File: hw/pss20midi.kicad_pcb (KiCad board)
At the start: 2 copper layers, 293.5 x 44 mm, 90 parts, among them J1 AVR-ISP, J2 Power in, J3 MIDI out, J4 keypad3, SW1 SW_Push, SW10 SW_Push, SW11 SW_Push, SW12 SW_Push, SW13 SW_Push, SW14 SW_Push, SW15 SW_Push, SW16 SW_Push, SW17 SW_Push, SW18 SW_Push, SW19 SW_Push, SW2 SW_Push, SW20 SW_Push, SW21 SW_Push, SW22 SW_Push, SW23 SW_Push, SW24 SW_Push, SW25 SW_Push, SW26 SW_Push, SW27 SW_Push, SW28 SW_Push, SW29 SW_Push, SW3 SW_Push, SW30 SW_Push, SW31 SW_Push, SW32 SW_Push, SW4 SW_Push, SW5 SW_Push, SW6 SW_Push, SW7 SW_Push, SW8 SW_Push, SW9 SW_Push, U1 ATmega328PB, U2 74HC153, U3 74HC153, U4 74HC153, U5 74HC153, U6 MAX232, Y1 4MHz

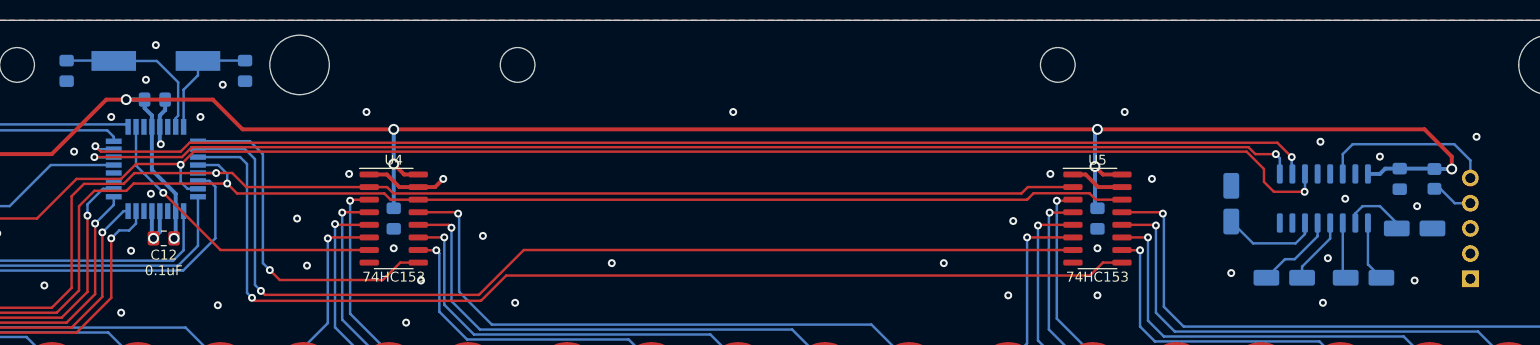
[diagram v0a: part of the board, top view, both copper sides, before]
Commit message: fixed MIDI voltage and polarity mistake
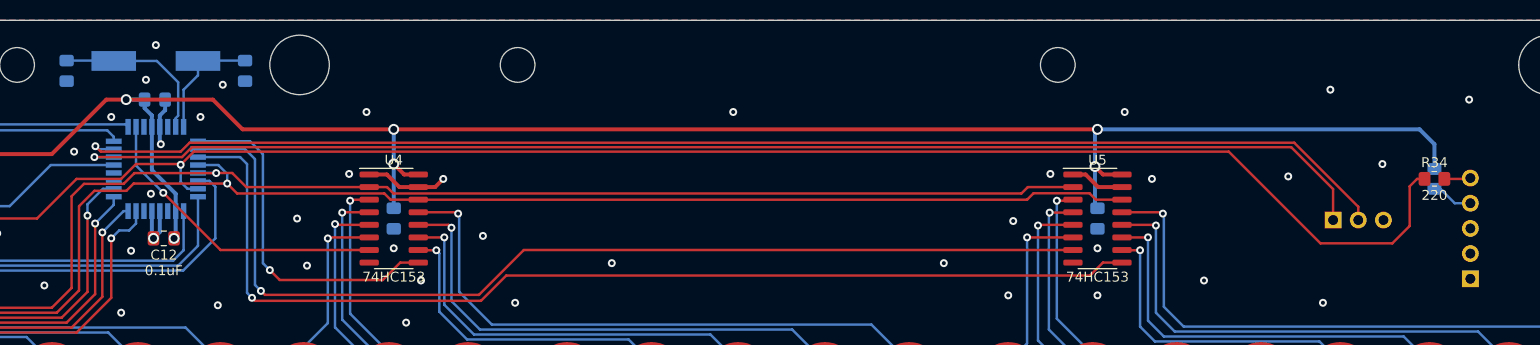
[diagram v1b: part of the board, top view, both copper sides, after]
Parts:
- removed C13: 0.1uF, Capacitor_SMD:C_0805_2012Metric_Pad1.18x1.45mm_HandSolder
- removed C3, C4, C5, C6: 1uF, Capacitor_SMD:CP_Elec_4x5.4
- removed U6: MAX232, Package_SO:SOIC-16_3.9x9.9mm_P1.27mm
- added J5: dbgcon, Connector_PinSocket_2.54mm:PinSocket_1x03_P2.54mm_Horizontal, B.Cu at (319.8, 126.2)
- added R34: 220, Resistor_SMD:R_0805_2012Metric_Pad1.20x1.40mm_HandSolder, F.Cu at (330.0, 122.0)
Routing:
- net /TXD1: track 148.3 -> 165.0 mm, vias 2 -> 1
- net /MIDI_TX: track 17.8 -> 2.66 mm
- net Net-(U6-VS-): track 9.85 -> 0.00 mm
- net VCC: track 625.0 -> 615.3 mm, vias 9 -> 8
- net /TXD0: track 125.6 -> 134.0 mm, vias 2 -> 1
- net Net-(U6-C2-): track 8.24 -> 0.00 mm
- net /RXD0: track 124.0 -> 132.2 mm, vias 2 -> 1
- net Net-(U6-VS+): track 6.71 -> 0.00 mm
- net Net-(U6-C2+): track 6.70 -> 0.00 mm
- net Net-(U6-C1+): track 6.09 -> 0.00 mm
- net Net-(U6-C1-): track 5.65 -> 0.00 mm
- net GND: vias 76 -> 73
